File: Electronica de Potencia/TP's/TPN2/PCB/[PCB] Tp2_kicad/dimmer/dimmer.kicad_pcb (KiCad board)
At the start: 2 copper layers, 65.8 x 49.5 mm, 17 parts, among them J1 Conn_01x02, J2 Conn_01x02, Q1 2N2646, Q2 TIC106

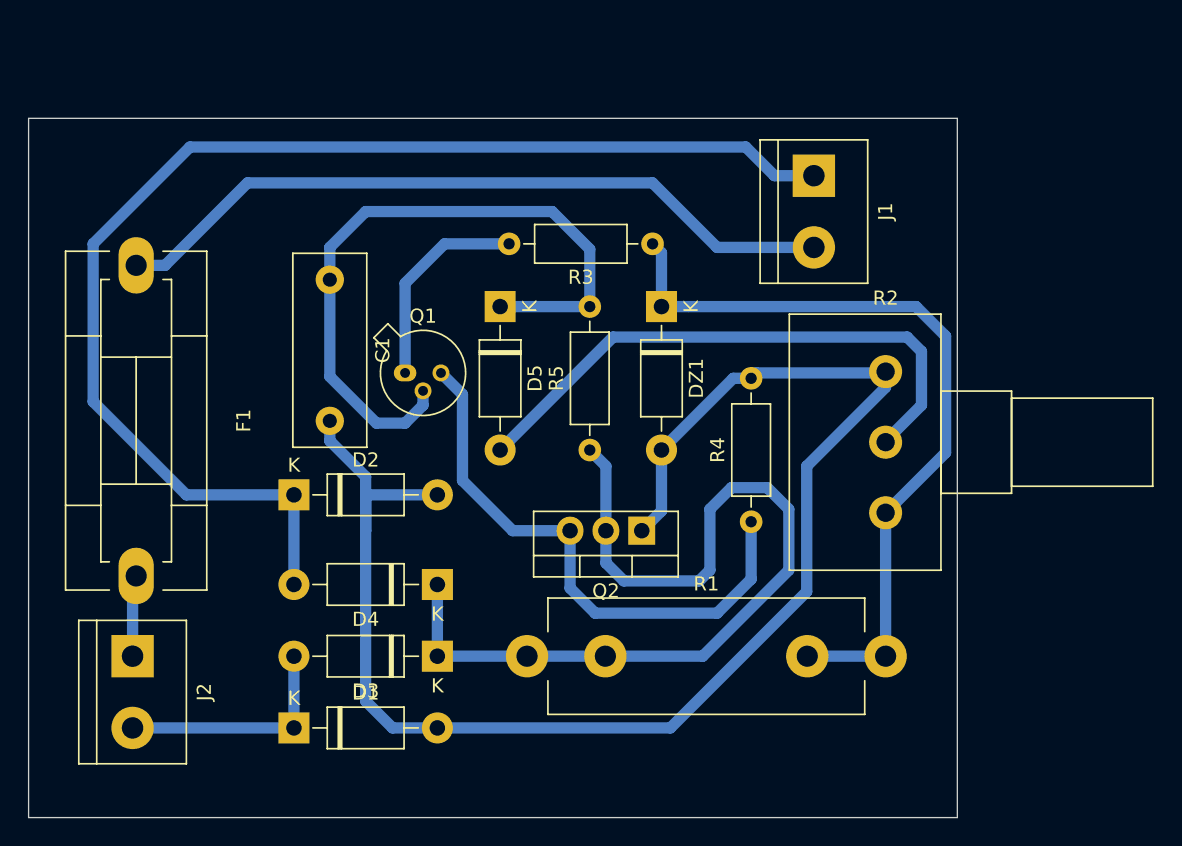
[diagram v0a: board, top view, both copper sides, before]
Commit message: Modularizo el proyecto para que sea portable para cualquiera, completo 3d's, me falta conseguir la Res de 5W para ver si corresponde el fp
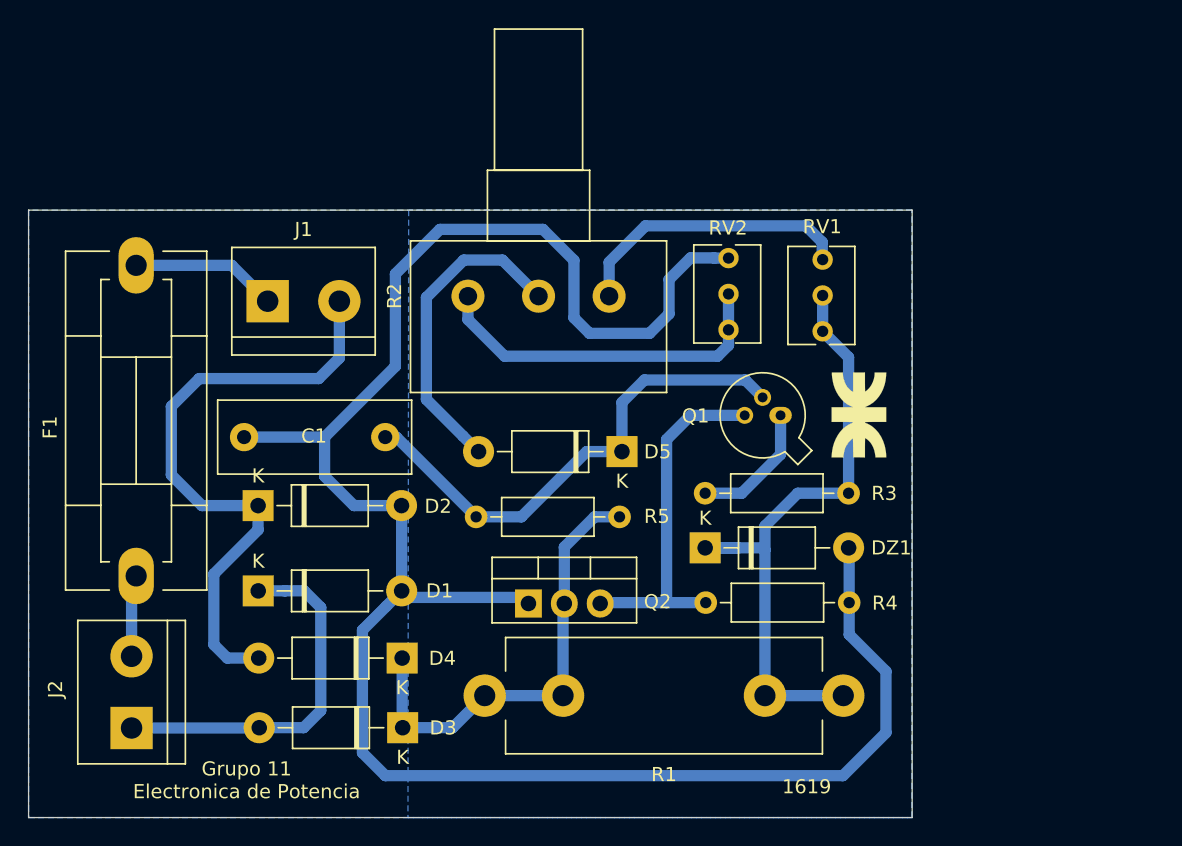
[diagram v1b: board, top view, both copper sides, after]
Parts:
- added G1: LOGO, lib_fp:logo_utn_fsilk_small, F.Cu at (178.4, 103.5)
- added RV1: R_POT_TRIM, lib_fp:Potentiometer_Bourns_3266Y_Vertical, F.Cu at (175.9, 97.6)
- added RV2: R_POT_TRIM, lib_fp:Potentiometer_Bourns_3266Y_Vertical, F.Cu at (169.2, 97.5)
- C1: footprint Capacitor_THT:C_Rect_L13.5mm_W5.0mm_P10.00mm_FKS3_FKP3_MKS4 -> lib_fp:C_Rect_L13.5mm_W5.0mm_P10.00mm_FKS3_FKP3_MKS4
- D1, D2, D3, D4, DZ1: footprint Diode_THT:D_DO-41_SOD81_P10.16mm_Horizontal -> lib_fp:D_DO-41_SOD81_P10.16mm_Horizontal
- D5: value 1N4007 -> 1N4001; footprint Diode_THT:D_DO-41_SOD81_P10.16mm_Horizontal -> lib_fp:D_DO-41_SOD81_P10.16mm_Horizontal
- F1: footprint Fuse_Holders_and_Fuses:Fuseholder5x20_horiz_SemiClosed_Casing10x25mm -> lib_fp:Fuseholder5x20_horiz_SemiClosed_Casing10x25mm
- J1: value Conn_01x02 -> Salida; footprint TerminalBlock:TerminalBlock_bornier-2_P5.08mm -> lib_fp:TerminalBlock_bornier-2_P5.08mm
- J2: value Conn_01x02 -> Entrada; footprint TerminalBlock:TerminalBlock_bornier-2_P5.08mm -> lib_fp:TerminalBlock_bornier-2_P5.08mm
- Q1: footprint Package_TO_SOT_THT:TO-18-3 -> lib_fp:TO-18-3
- Q2: footprint Package_TO_SOT_THT:TO-220-3_Vertical -> lib_fp:TO-220-3_Vertical
- R1: footprint Resistor_THT:R_Axial_Shunt_L22.2mm_W8.0mm_PS14.30mm_P25.40mm -> lib_fp:R_Axial_Shunt_L22.2mm_W8.0mm_PS14.30mm_P25.40mm
- R2: footprint Potentiometer_THT:Potentiometer_Alps_RK163_Single_Horizontal -> lib_fp:Potentiometer_Alps_RK163_Single_Horizontal
- R3, R4, R5: footprint Resistor_THT:R_Axial_DIN0207_L6.3mm_D2.5mm_P10.16mm_Horizontal -> lib_fp:R_Axial_DIN0207_L6.3mm_D2.5mm_P10.16mm_Horizontal
- moved J1 39.7 mm to (136.6, 95.5), turned to 0 degrees
- moved Q1 26.8 mm to (172.9, 103.6), turned to 180 degrees
- moved R2 24.9 mm to (160.8, 95.1), turned to 90 degrees
- moved R3 22.5 mm to (177.7, 109.1)
- moved DZ1 17.4 mm to (167.6, 113.0), turned to 0 degrees
- moved D5 13.4 mm to (161.7, 106.2), turned to 180 degrees
- moved C1 11.8 mm to (144.9, 105.1), turned to 180 degrees
- moved D1 10.0 mm to (135.9, 116.0)
- moved Q2 9.54 mm to (155.0, 116.9), turned to 0 degrees
- moved R4 6.57 mm to (167.6, 116.9), turned to 0 degrees
- moved D4 5.78 mm to (146.1, 120.8)
- moved D3 5.63 mm to (146.1, 125.7)
- moved R5 5.18 mm to (161.5, 110.8), turned to 180 degrees
- moved J2 5.09 mm to (126.9, 125.7), turned to 90 degrees
- moved R1 4.10 mm to (151.9, 123.4)
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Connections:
- J1 pad 1: GND -> Net-(F1-Pad1)
- J1 pad 2: Net-(F1-Pad1) -> GND
- J2 pad 1: Net-(F1-Pad2) -> Net-(D1-Pad1)
- J2 pad 2: Net-(D1-Pad1) -> Net-(F1-Pad2)
- Q2 pad 2: Net-(D3-Pad1) -> Net-(Q2-Pad2)
- R2 pad 1: Net-(DZ1-Pad1) -> Net-(R2-Pad1)
- R2 pad 3: Net-(C1-Pad2) -> Net-(R2-Pad3)
- R4 pad 2: Net-(C1-Pad2) -> Net-(R4-Pad2)
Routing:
- net GND: track 89.2 -> 44.0 mm
- net Net-(F1-Pad1): track 52.3 -> 10.4 mm
- net Net-(C1-Pad2): track 106.9 -> 143.6 mm
- net Net-(D3-Pad1): track 64.7 -> 32.6 mm
- net Net-(R2-Pad3): track 0.00 -> 25.1 mm
- net Net-(R2-Pad1): track 0.00 -> 20.3 mm
- net Net-(D5-Pad2): track 41.1 -> 22.6 mm
- net Net-(Q1-Pad3): track 40.0 -> 25.3 mm
- net Net-(C1-Pad1): track 49.6 -> 35.6 mm
- net Net-(DZ1-Pad1): track 55.7 -> 45.9 mm
- net Net-(D1-Pad1): track 16.5 -> 26.1 mm
- net Net-(Q1-Pad1): track 14.9 -> 9.25 mm
- added copper zone on B.Cu, net (none)
- added copper zone on B.Cu, net GND
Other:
- board size 65.8 x 49.5 mm -> 62.6 x 43 mm
- board text added: "1619"
- board text added: "Grupo 11 Electronica de Potencia"

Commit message: Arreglo footprint de UJT
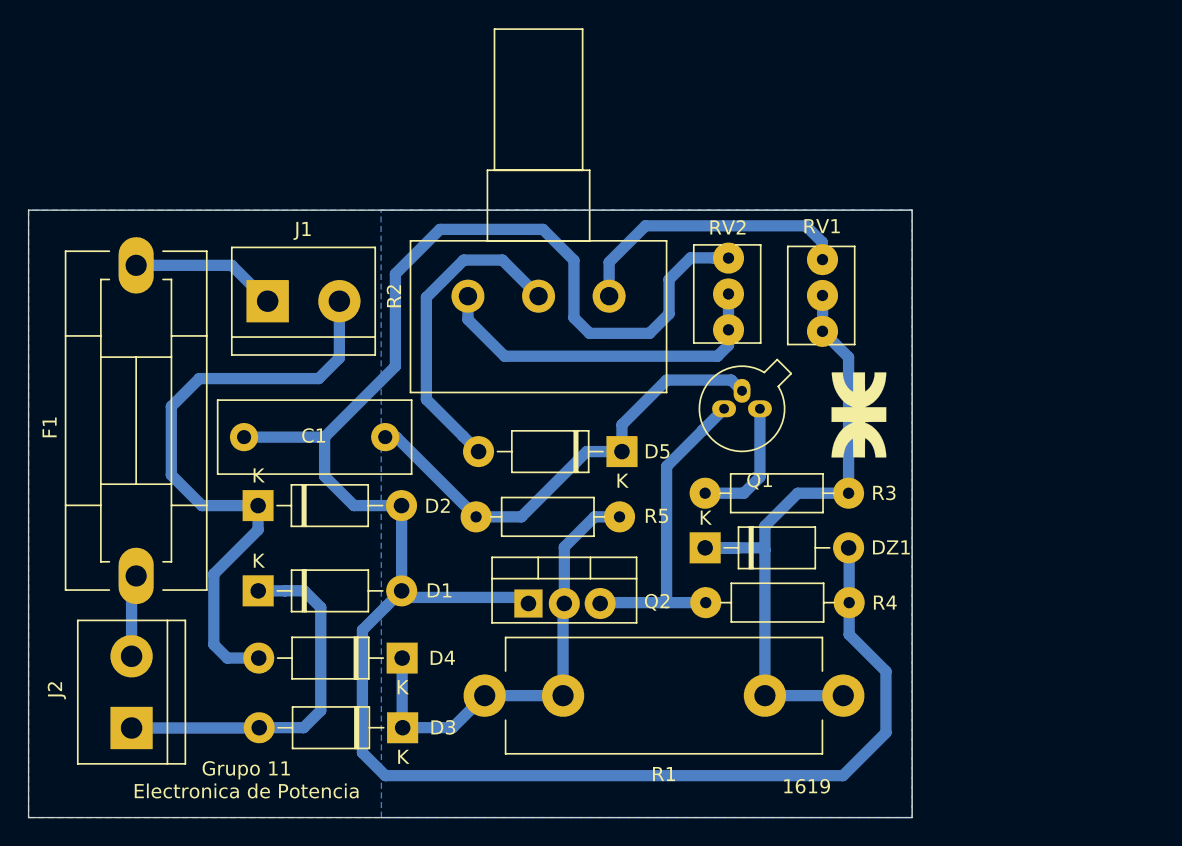
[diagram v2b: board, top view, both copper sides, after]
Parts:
- D5: value 1N4001 -> 1N4007
- J1: value Salida -> Conn_01x02
- J2: value Entrada -> Conn_01x02
- Q1: value 2N2646 -> 2N2647
- moved Q1 1.53 mm to (171.4, 103.1)
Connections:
- Q1 pad 1: Net-(Q1-Pad1) -> Net-(C1-Pad1)
- Q1 pad 2: Net-(C1-Pad1) -> Net-(Q1-Pad2)
- Q2 pad 2: Net-(Q2-Pad2) -> Net-(D3-Pad1)
- Q2 pad 3: Net-(Q1-Pad3) -> Net-(Q1-Pad2)
- R3 pad 2: Net-(Q1-Pad1) -> Net-(Q1-Pad3)
- R4 pad 1: Net-(Q1-Pad3) -> Net-(Q1-Pad2)
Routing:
- net Net-(Q1-Pad2): track 0.00 -> 22.9 mm
- net Net-(Q1-Pad3): track 25.3 -> 9.19 mm
- net Net-(Q1-Pad1): track 9.25 -> 0.00 mm
- net Net-(C1-Pad1): track 35.6 -> 33.1 mm

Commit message: Arreglando a little bit
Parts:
- DZ1: value 1N47xxA -> Diode_1N47xxA
- moved DZ1 11.5 mm to (178.4, 116.8), turned to 180 degrees
- moved R4 4.03 mm to (168.0, 112.9)
- moved G1 1.48 mm to (177.3, 102.6)
- moved R3 0.49 mm to (178.2, 109.2)
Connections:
- R4 pad 2: Net-(R4-Pad2) -> Net-(C1-Pad2)
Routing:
- net Net-(DZ1-Pad1): track 45.9 -> 39.8 mm
- net Net-(C1-Pad2): track 143.6 -> 138.6 mm
- net Net-(Q1-Pad3): track 9.19 -> 8.20 mm
- net Net-(Q1-Pad2): track 22.9 -> 22.3 mm
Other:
- net class Default: clearance 0.4 -> 0.2
- rule trace_clearance: 0.4 -> 0.2
